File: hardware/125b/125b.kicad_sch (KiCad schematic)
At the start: 51 parts, among them J1 Guitar in, J10 Barrel_Jack, J11 NRJ6HF, SW1 Switch 1, SW2 Switch 2, SW3 RotaryEncoder_Switch, SW4 SW_DIP_x02, U1 TL074, U2 L78L05_TO92

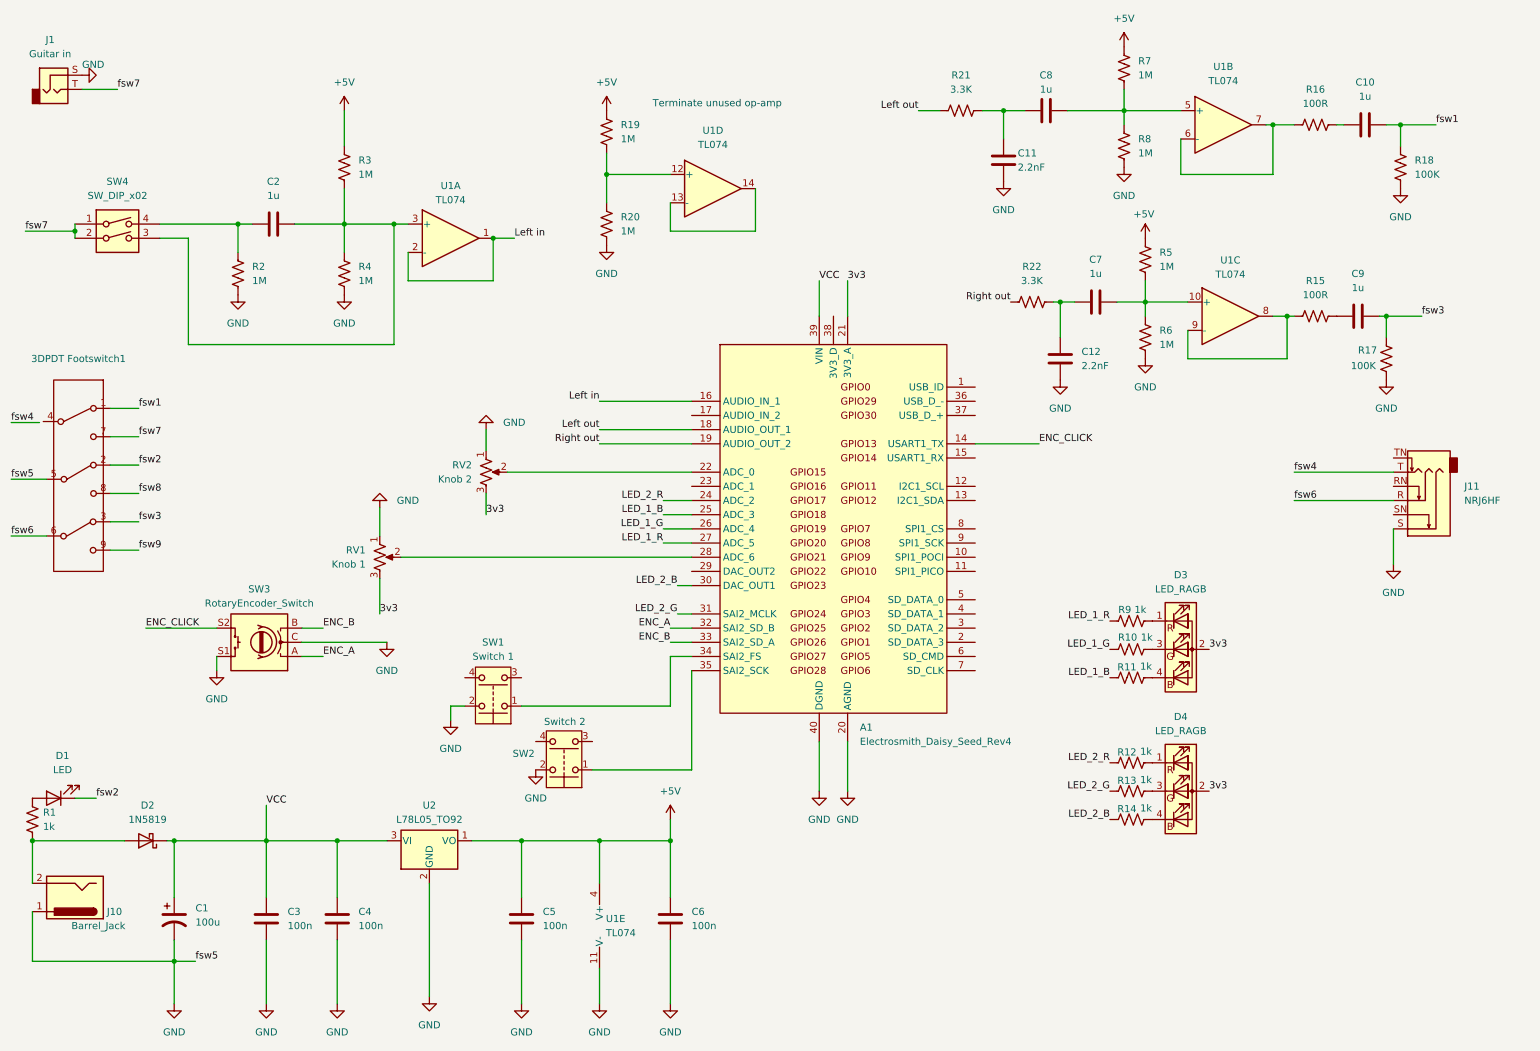
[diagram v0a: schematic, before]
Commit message: Add schematic and pcb files for footswitch board
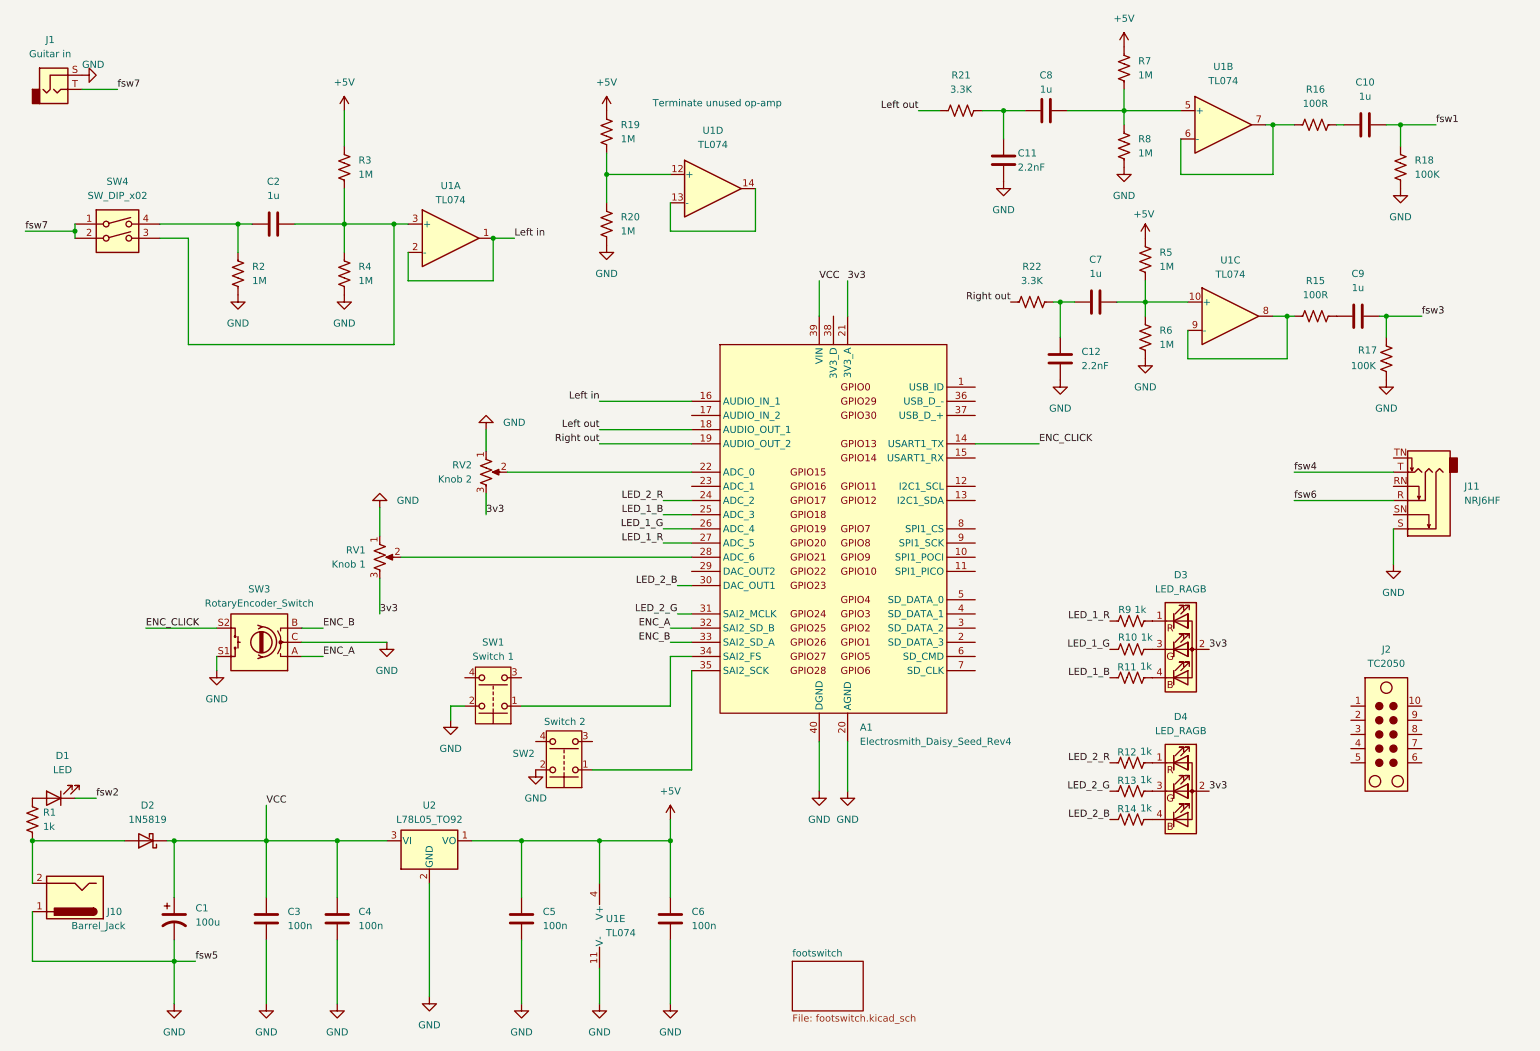
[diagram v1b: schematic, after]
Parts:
- removed 3DPDT Footswitch1: ~, symbol Switch:SW_3DPDT
- added J2: TC2050, Connector_IDC:IDC-Header_2x05_P2.54mm_Vertical, symbol Connector:TC2050
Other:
- added sheet footswitch (footswitch.kicad_sch)
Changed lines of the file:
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@@
 	(wire
 		(pts
-			(xy 33.02 93.98) (xy 38.1 93.98)
-		)
-		(stroke
-			(width 0)
-			(type default)
-		)
-	)
-	(wire
-		(pts
 			(xy 73.66 179.07) (xy 73.66 190.5)
 		)
@@
 	(wire
 		(pts
-			(xy 33.02 88.9) (xy 38.1 88.9)
-		)
-		(stroke
-			(width 0)
-			(type default)
-		)
-	)
-	(wire
-		(pts
 			(xy 264.16 33.02) (xy 264.16 36.83)
 		)
@@
 	(wire
 		(pts
-			(xy 15.24 106.68) (xy 21.59 106.68)
-		)
-		(stroke
-			(width 0)
-			(type default)
-		)
-	)
-	(wire
-		(pts
 			(xy 74.93 30.48) (xy 74.93 36.83)
 		)
@@
 	(wire
 		(pts
-			(xy 33.02 99.06) (xy 38.1 99.06)
-		)
-		(stroke
-			(width 0)
-			(type default)
-		)
-	)
-	(wire
-		(pts
 			(xy 133.35 125.73) (xy 137.16 125.73)
 		)
@@
 	(wire
 		(pts
-			(xy 15.24 96.52) (xy 21.59 96.52)
-		)
-		(stroke
-			(width 0)
-			(type default)
-		)
-	)
-	(wire
-		(pts
 			(xy 243.84 67.31) (xy 245.11 67.31)
 		)
@@
 	(wire
 		(pts
-			(xy 33.02 104.14) (xy 38.1 104.14)
-		)
-		(stroke
-			(width 0)
-			(type default)
-		)
-	)
-	(wire
-		(pts
 			(xy 96.52 137.16) (xy 93.98 137.16)
 		)
@@
 	(wire
 		(pts
-			(xy 33.02 83.82) (xy 38.1 83.82)
-		)
-		(stroke
-			(width 0)
-			(type default)
-		)
-	)
-	(wire
-		(pts
 			(xy 201.93 64.77) (xy 203.2 64.77)
 		)
@@
 	(wire
 		(pts
-			(xy 15.24 86.36) (xy 20.32 86.36)
-		)
-		(stroke
-			(width 0)
-			(type default)
-		)
-	)
-	(wire
-		(pts
 			(xy 120.65 184.15) (xy 120.65 190.5)
 		)
@@
 		)
 	)
-	(wire
-		(pts
-			(xy 33.02 109.22) (xy 38.1 109.22)
-		)
-		(stroke
-			(width 0)
-			(type default)
-		)
-	)
 	(label "VCC"
 		(at 160.02 60.96 0)
@@
 		)
 	)
-	(label "fsw8"
-		(at 38.1 99.06 0)
-		(effects
-			(font
-				(size 1.27 1.27)
-			)
-			(justify left bottom)
-		)
-	)
 	(label "3v3"
 		(at 229.87 152.4 0)
@@
 		)
 	)
-	(label "fsw1"
-		(at 38.1 83.82 0)
-		(effects
-			(font
-				(size 1.27 1.27)
-			)
-			(justify left bottom)
-		)
-	)
 	(label "LED_2_G"
 		(at 212.09 152.4 180)
@@
 	)
 	(label "fsw4"
-		(at 15.24 86.36 0)
-		(effects
-			(font
-				(size 1.27 1.27)
-			)
-			(justify left bottom)
-		)
-	)
-	(label "fsw9"
-		(at 38.1 109.22 0)
-		(effects
-			(font
-				(size 1.27 1.27)
-			)
-			(justify left bottom)
-		)
-	)
-	(label "fsw4"
 		(at 245.11 95.25 0)
 		(effects
@@
 		)
 	)
-	(label "fsw6"
-		(at 15.24 106.68 0)
-		(effects
-			(font
-				(size 1.27 1.27)
-			)
-			(justify left bottom)
-		)
-	)
 	(label "fsw5"
 		(at 48.26 182.88 0)
@@
 		)
 	)
-	(label "fsw5"
-		(at 15.24 96.52 0)
-		(effects
-			(font
-				(size 1.27 1.27)
-			)
-			(justify left bottom)
-		)
-	)
-	(label "fsw7"
-		(at 38.1 88.9 0)
-		(effects
-			(font
-				(size 1.27 1.27)
-			)
-			(justify left bottom)
-		)
-	)
 	(label "Left in"
 		(at 120.65 82.55 180)
@@
 		)
 	)
-	(label "fsw2"
-		(at 38.1 93.98 0)
-		(effects
-			(font
-				(size 1.27 1.27)
-			)
-			(justify left bottom)
-		)
-	)
 	(label "LED_1_G"
 		(at 212.09 127 180)
@@
 		)
 	)
-	(label "fsw3"
-		(at 38.1 104.14 0)
-		(effects
-			(font
-				(size 1.27 1.27)
-			)
-			(justify left bottom)
-		)
-	)
 	(label "3v3"
 		(at 229.87 127 0)
@@
 	)
 	(symbol
+		(lib_id "Connector:TC2050")
+		(at 260.35 142.24 0)
+		(unit 1)
+		(exclude_from_sim no)
+		(in_bom no)
+		(on_board yes)
+		(dnp no)
+		(fields_autoplaced yes)
+		(property "Reference" "J2"
+			(at 261.62 127 0)
+			(effects
+				(font
+					(size 1.27 1.27)
+				)
+			)
+		)
+		(property "Value" "TC2050"
+			(at 261.62 129.54 0)
+			(effects
+				(font
+					(size 1.27 1.27)
+				)
+			)
+		)
+		(property "Footprint" "Connector_IDC:IDC-Header_2x05_P2.54mm_Vertical"
+			(at 261.62 142.24 0)
+			(effects
+				(font
+					(size 1.27 1.27)
+				)
+				(hide yes)
+			)
+		)
+		(property "Datasheet" "https://www.tag-connect.com/wp-content/uploads/bsk-pdf-manager/TC2050-IDC-NL_Datasheet_8.pdf"
+			(at 261.62 142.24 0)
+			(effects
+				(font
+					(size 1.27 1.27)
+				)
+				(hide yes)
+			)
+		)
+		(property "Description" "Tag-Connect’s 10-pins connector"
+			(at 260.35 142.24 0)
+			(effects
+				(font
+					(size 1.27 1.27)
+				)
+				(hide yes)
+			)
+		)
+		(pin "1"
+		)
+		(pin "6"
+		)
+		(pin "2"
+		)
+		(pin "10"
+		)
+		(pin "9"
+		)
+		(pin "8"
+		)
+		(pin "7"
+		)
+		(pin "5"
+		)
+		(pin "4"
+		)
+		(pin "3"
+		)
+		(instances
+			(project ""
+				(path "/12e895f7-e5ae-4934-aed6-e6e04c63dd03"
+					(reference "J2")
+					(unit 1)
+				)
+			)
+		)
+	)
+	(symbol
 		(lib_name "GND_16")
 		(lib_id "power:GND")
@@
 		)
 	)
-	(symbol
-		(lib_id "Switch:SW_3DPDT")
-		(at 27.94 95.25 0)
-		(unit 1)
+	(sheet
+		(at 155.194 182.88)
+		(size 12.7 8.89)
 		(exclude_from_sim no)
 		(in_bom yes)
@@
 		(dnp no)
 		(fields_autoplaced yes)
-		(property "Reference" "3DPDT Footswitch1"
-			(at 27.305 74.93 0)
-			(effects
-				(font
-					(size 1.27 1.27)
-				)
-			)
+		(stroke
+			(width 0.1524)
+			(type solid)
 		)
-		(property "Value" "~"
-			(at 27.305 77.47 0)
-			(effects
-				(font
-					(size 1.27 1.27)
-				)
-			)
+		(fill
+			(color 0 0 0 0.0000)
 		)
-		(property "Footprint" ""
-			(at 27.94 95.25 0)
+		(property "Sheetname" "footswitch"
+			(at 155.194 182.1684 0)
 			(effects
 				(font
 					(size 1.27 1.27)
 				)
-				(hide yes)
-			)
-		)
-		(property "Datasheet" ""
-			(at 27.94 95.25 0)
-			(effects
-				(font
-					(size 1.27 1.27)
-				)
-				(hide yes)
+				(justify left bottom)
 			)
 		)
-		(property "Description" ""
-			(at 27.94 95.25 0)
+		(property "Sheetfile" "footswitch.kicad_sch"
+			(at 155.194 192.3546 0)
 			(effects
 				(font
 					(size 1.27 1.27)
 				)
-				(hide yes)
+				(justify left top)
 			)
 		)
-		(pin "4"
-		)
-		(pin "5"
-		)
-		(pin "6"
-		)
-		(pin "1"
-		)
-		(pin "7"
-		)
-		(pin "2"
-		)
-		(pin "8"
-		)
-		(pin "3"
-		)
-		(pin "9"
-		)
 		(instances
-			(project ""
+			(project "125b"
 				(path "/12e895f7-e5ae-4934-aed6-e6e04c63dd03"
-					(reference "3DPDT Footswitch1")
-					(unit 1)
+					(page "2")
 				)
 			)

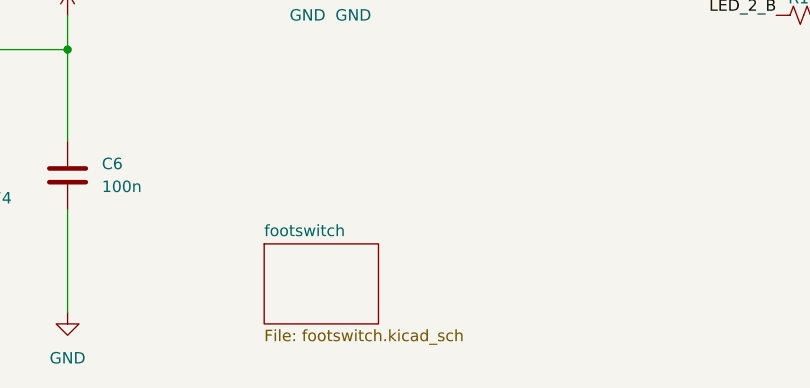
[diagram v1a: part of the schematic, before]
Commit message: New project for the footswitch board
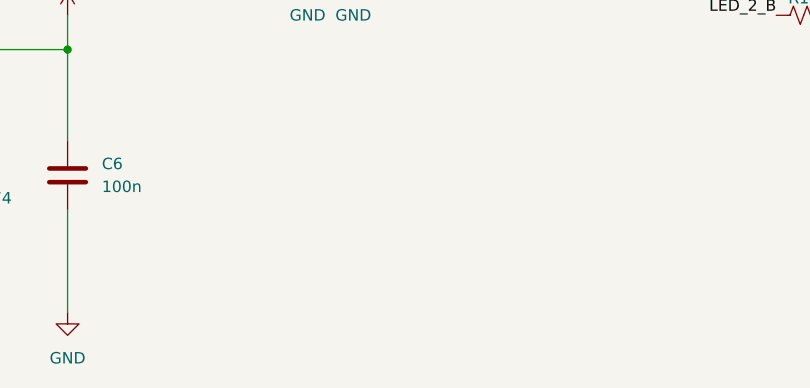
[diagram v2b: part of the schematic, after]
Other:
- removed sheet footswitch
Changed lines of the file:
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@@
-		)
-	)
-	(sheet
-		(at 155.194 182.88)
-		(size 12.7 8.89)
-		(exclude_from_sim no)
-		(in_bom yes)
-		(on_board yes)
-		(dnp no)
-		(fields_autoplaced yes)
-		(stroke
-			(width 0.1524)
-			(type solid)
-		)
-		(fill
-			(color 0 0 0 0.0000)
-		)
-		(property "Sheetname" "footswitch"
-			(at 155.194 182.1684 0)
-			(effects
-				(font
-					(size 1.27 1.27)
-				)
-				(justify left bottom)
-			)
-		)
-		(property "Sheetfile" "footswitch.kicad_sch"
-			(at 155.194 192.3546 0)
-			(effects
-				(font
-					(size 1.27 1.27)
-				)
-				(justify left top)
-			)
-		)
-		(instances
-			(project "125b"
-				(path "/12e895f7-e5ae-4934-aed6-e6e04c63dd03"
-					(page "2")
-				)
-			)
 		)
 	)

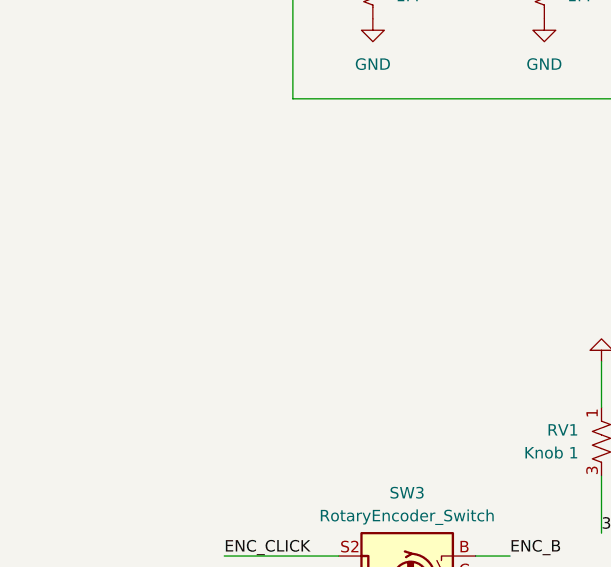
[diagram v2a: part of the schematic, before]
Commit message: Wider traces for footswitch PCB and connect main board
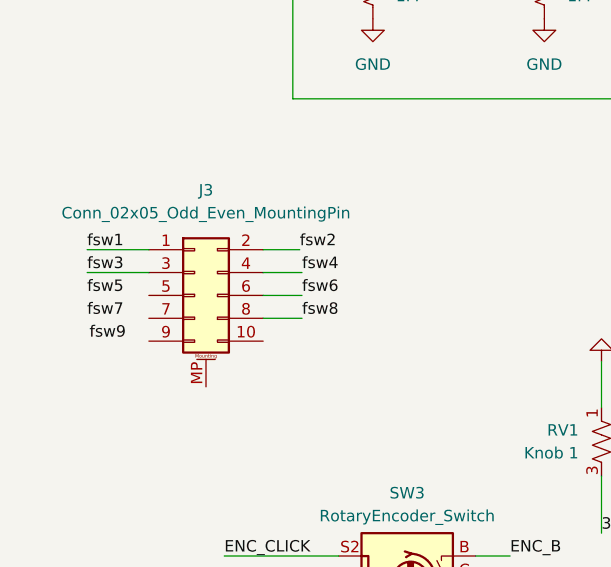
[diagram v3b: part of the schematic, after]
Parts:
- added J3: Conn_02x05_Odd_Even_MountingPin, symbol Connector_Generic_MountingPin:Conn_02x05_Odd_Even_MountingPin
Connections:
- net fsw1: now also J3.1 (Pin_1)
- net fsw2: now also J3.2 (Pin_2)
- net fsw3: now also J3.3 (Pin_3)
- net fsw4: now also J3.4 (Pin_4)
- net fsw6: now also J3.6 (Pin_6)
- new net fsw8: J3.8 (Pin_8)
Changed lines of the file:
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@@
 	(wire
 		(pts
+			(xy 43.688 96.774) (xy 48.006 96.774)
+		)
+		(stroke
+			(width 0)
+			(type default)
+		)
+	)
+	(wire
+		(pts
 			(xy 74.93 50.8) (xy 74.93 55.88)
 		)
@@
 	(wire
 		(pts
+			(xy 43.688 91.694) (xy 48.006 91.694)
+		)
+		(stroke
+			(width 0)
+			(type default)
+		)
+	)
+	(wire
+		(pts
 			(xy 132.08 102.87) (xy 137.16 102.87)
 		)
@@
 	(wire
 		(pts
+			(xy 24.13 89.154) (xy 30.988 89.154)
+		)
+		(stroke
+			(width 0)
+			(type default)
+		)
+	)
+	(wire
+		(pts
 			(xy 46.99 72.39) (xy 83.82 72.39)
 		)
@@
 	(wire
 		(pts
+			(xy 43.688 94.234) (xy 48.006 94.234)
+		)
+		(stroke
+			(width 0)
+			(type default)
+		)
+	)
+	(wire
+		(pts
 			(xy 121.92 41.91) (xy 121.92 46.99)
 		)
@@
 	(wire
 		(pts
+			(xy 24.13 91.694) (xy 30.988 91.694)
+		)
+		(stroke
+			(width 0)
+			(type default)
+		)
+	)
+	(wire
+		(pts
 			(xy 106.68 137.16) (xy 133.35 137.16)
 		)
@@
 		)
 	)
+	(wire
+		(pts
+			(xy 43.688 89.154) (xy 47.752 89.154)
+		)
+		(stroke
+			(width 0)
+			(type default)
+		)
+	)
 	(label "VCC"
 		(at 160.02 60.96 0)
@@
 		)
 	)
+	(label "fsw6"
+		(at 48.006 94.234 0)
+		(effects
+			(font
+				(size 1.27 1.27)
+			)
+			(justify left bottom)
+		)
+	)
 	(label "Right out"
 		(at 120.65 90.17 180)
@@
 		)
 	)
+	(label "fsw3"
+		(at 24.13 91.694 0)
+		(effects
+			(font
+				(size 1.27 1.27)
+			)
+			(justify left bottom)
+		)
+	)
 	(label "LED_2_G"
 		(at 212.09 152.4 180)
@@
 		)
 	)
+	(label "fsw5"
+		(at 24.13 94.234 0)
+		(effects
+			(font
+				(size 1.27 1.27)
+			)
+			(justify left bottom)
+		)
+	)
 	(label "fsw1"
 		(at 270.51 33.02 0)
@@
 		)
 	)
+	(label "fsw2"
+		(at 47.752 89.154 0)
+		(effects
+			(font
+				(size 1.27 1.27)
+			)
+			(justify left bottom)
+		)
+	)
 	(label "LED_2_G"
 		(at 134.62 120.65 180)
@@
 		)
 	)
+	(label "fsw1"
+		(at 24.13 89.154 0)
+		(effects
+			(font
+				(size 1.27 1.27)
+			)
+			(justify left bottom)
+		)
+	)
 	(label "LED_1_R"
 		(at 132.08 107.95 180)
@@
 		)
 	)
+	(label "fsw9"
+		(at 24.384 99.314 0)
+		(effects
+			(font
+				(size 1.27 1.27)
+			)
+			(justify left bottom)
+		)
+	)
 	(label "LED_1_R"
 		(at 212.09 121.92 180)
@@
 		)
 	)
+	(label "fsw7"
+		(at 24.13 96.774 0)
+		(effects
+			(font
+				(size 1.27 1.27)
+			)
+			(justify left bottom)
+		)
+	)
 	(label "Left in"
 		(at 120.65 82.55 180)
@@
 		)
 	)
+	(label "fsw4"
+		(at 48.006 91.694 0)
+		(effects
+			(font
+				(size 1.27 1.27)
+			)
+			(justify left bottom)
+		)
+	)
+	(label "fsw8"
+		(at 48.006 96.774 0)
+		(effects
+			(font
+				(size 1.27 1.27)
+			)
+			(justify left bottom)
+		)
+	)
 	(label "ENC_A"
 		(at 133.35 123.19 180)
@@
 					(unit 1)
 				)
+			)
+		)
+	)
+	(symbol
+		(lib_id "Connector_Generic_MountingPin:Conn_02x05_Odd_Even_MountingPin")
+		(at 36.068 94.234 0)
+		(unit 1)
+		(exclude_from_sim no)
+		(in_bom yes)
+		(on_board yes)
+		(dnp no)
+		(fields_autoplaced yes)
+		(property "Reference" "J3"
+			(at 37.338 82.55 0)
+			(effects
+				(font
+					(size 1.27 1.27)
+				)
+			)
+		)
+		(property "Value" "Conn_02x05_Odd_Even_MountingPin"
+			(at 37.338 85.09 0)
+			(effects
+				(font
+					(size 1.27 1.27)
+				)
+			)
+		)
+		(property "Footprint" ""
+			(at 36.068 94.234 0)
+			(effects
+				(font
+					(size 1.27 1.27)
+				)
+				(hide yes)
+			)
+		)
+		(property "Datasheet" "~"
+			(at 36.068 94.234 0)
+			(effects
+				(font
+					(size 1.27 1.27)
+				)
+				(hide yes)
+			)
+		)
+		(property "Description" "Generic connectable mounting pin connector, double row, 02x05, odd/even pin numbering scheme (row 1 odd numbers, row 2 even numbers), script generated (kicad-library-utils/schlib/autogen/connector/)"
+			(at 36.068 94.234 0)
+			(effects
+				(font
+					(size 1.27 1.27)
+				)
+				(hide yes)
+			)
+		)
+		(pin "1"
+		)
+		(pin "3"
+		)
+		(pin "5"
+		)
+		(pin "7"
+		)
+		(pin "9"
+		)
+		(pin "MP"
+		)
+		(pin "2"
+		)
+		(pin "4"
+		)
+		(pin "6"
+		)
+		(pin "8"
+		)
+		(pin "10"
+		)
+		(instances
+			(project ""
+				(path "/12e895f7-e5ae-4934-aed6-e6e04c63dd03"
+					(reference "J3")
+					(unit 1)
+				)
